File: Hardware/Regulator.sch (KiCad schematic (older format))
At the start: 8 parts, among them U2 LM1084IS-3.3/NOPB, U3 LM1084IS-5.0/NOPB

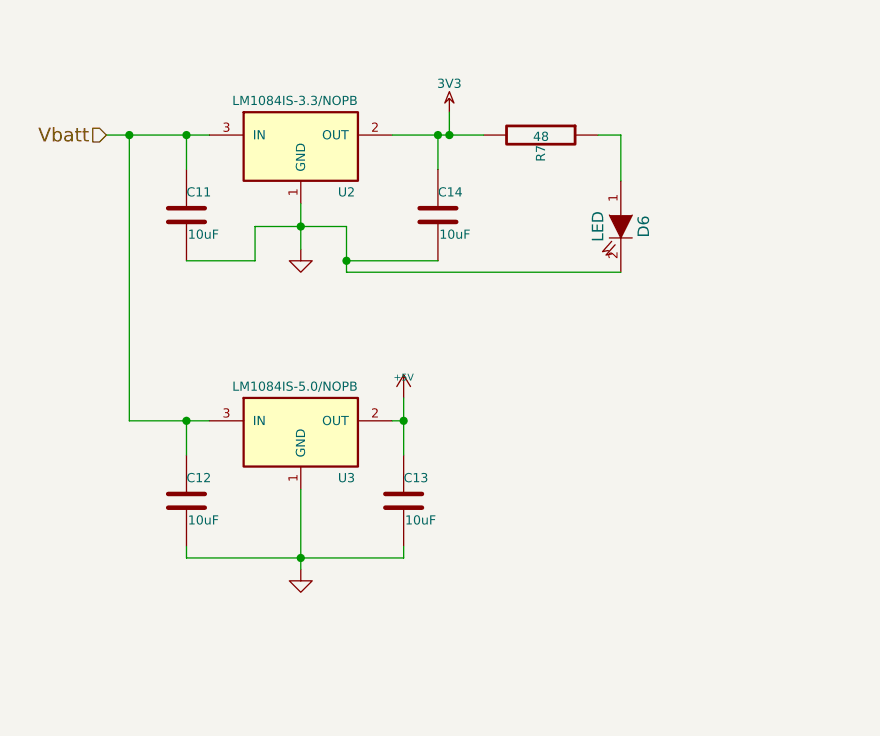
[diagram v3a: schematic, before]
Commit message: Finished schematic work. Began footprints
Began assigning footprints for R2
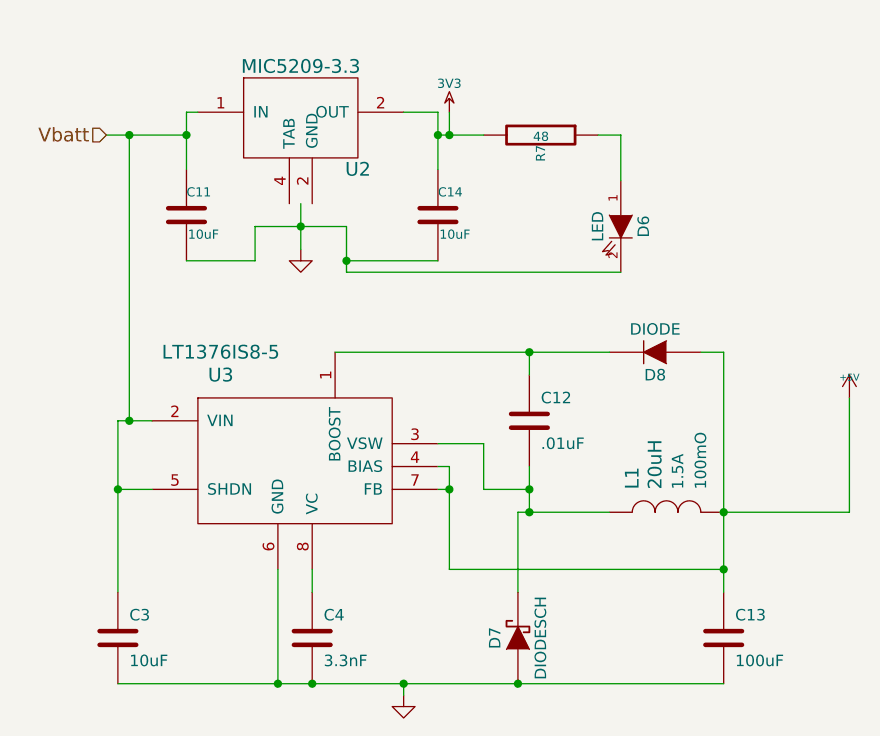
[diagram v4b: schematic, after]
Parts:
- removed U2: LM1084IS-3.3/NOPB, SMD_Packages:DPAK-3, symbol LM1084IS-3.3/NOPB
- removed U3: LM1084IS-5.0/NOPB, SMD_Packages:DPAK-3, symbol LM1084IS-5.0/NOPB
- added C3: 10uF, Capacitors_SMD:C_0805_HandSoldering, symbol C
- added C4: 3.3nF, Capacitors_SMD:C_0805_HandSoldering, symbol C
- added D7: DIODESCH, Diodes_SMD:Diode-MELF_Handsoldering, symbol DIODESCH
- added D8: DIODE, Diodes_SMD:Diode-MELF_Handsoldering, symbol DIODE
- added L1: 20uH, Capacitors_SMD:C_2220_HandSoldering, symbol Inductor
- added U2: MIC5209-3.3, SMD_Packages:DPAK-3, symbol MIC5209-3.3
- added U3: LT1376IS8-5, SMD_Packages:DPAK-3, symbol LT1376IS8-5
- C12: value 10uF -> .01uF
- C13: value 10uF -> 100uF
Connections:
- net +5V: now also D8.1 (A), L1.2, U3.4 (BIAS), U3.7 (FB)
- net 3V3: now also U2.2 (OUT)
- net GND: now also C3.2, C4.2, D7.1 (A), U3.6 (GND); no longer C12.2
- net Vbatt: now also C3.1, U2.1 (IN), U3.2 (VIN), U3.5 (SHDN); no longer C12.1
- new net: C12.2, D7.2 (K), L1.1, U3.3 (VSW)
- new net: C12.1, D8.2 (K), U3.1 (BOOST)
- new net: C4.1, U3.8 (VC)
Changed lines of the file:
@@
 $EndDescr
 $Comp
-L 3V3 #PWR018
+L 3V3 #PWR019
 U 1 1 543769E5
 P 2300 2050
-F 0 "#PWR018" H 2300 2150 40  0001 C CNN
+F 0 "#PWR019" H 2300 2150 40  0001 C CNN
 F 1 "3V3" H 2300 2175 40  0000 C CNN
 F 2 "" H 2300 2050 60  0000 C CNN
@@
 	1    0    0    -1
 $EndComp
-$Comp
-L LM1084IS-3.3/NOPB U2
-U 1 1 543769F9
-P 1650 2200
-F 0 "U2" H 1850 2000 40  0000 C CNN
-F 1 "LM1084IS-3.3/NOPB" H 1350 2400 40  0000 L CNN
-F 2 "SMD_Packages:DPAK-3" H 1650 2300 30  0001 C CIN
-F 3 "" H 1650 2200 60  0000 C CNN
-	1    1650 2200
-	1    0    0    -1
-$EndComp
 Text HLabel 800  2150 0    60   Input ~ 0
 Vbatt
 $Comp
-L GND #PWR019
+L GND #PWR020
 U 1 1 54376AC4
 P 1650 2650
-F 0 "#PWR019" H 1650 2650 30  0001 C CNN
+F 0 "#PWR020" H 1650 2650 30  0001 C CNN
 F 1 "GND" H 1650 2580 30  0001 C CNN
 F 2 "" H 1650 2650 60  0000 C CNN
@@
 $EndComp
 $Comp
-L LM1084IS-5.0/NOPB U3
-U 1 1 5444771F
-P 1650 3450
-F 0 "U3" H 1850 3250 40  0000 C CNN
-F 1 "LM1084IS-5.0/NOPB" H 1350 3650 40  0000 L CNN
-F 2 "SMD_Packages:DPAK-3" H 1650 3550 30  0001 C CIN
-F 3 "~" H 1650 3450 60  0000 C CNN
-	1    1650 3450
-	1    0    0    -1
-$EndComp
-$Comp
-L C C12
-U 1 1 5444778F
-P 1150 3750
-F 0 "C12" H 1150 3850 40  0000 L CNN
-F 1 "10uF" H 1156 3665 40  0000 L CNN
-F 2 "Capacitors_SMD:C_0805_HandSoldering" H 1188 3600 30  0001 C CNN
-F 3 "" H 1150 3750 60  0000 C CNN
-	1    1150 3750
-	1    0    0    -1
-$EndComp
-$Comp
-L GND #PWR020
-U 1 1 544477E3
-P 1650 4050
-F 0 "#PWR020" H 1650 4050 30  0001 C CNN
-F 1 "GND" H 1650 3980 30  0001 C CNN
-F 2 "" H 1650 4050 60  0000 C CNN
-F 3 "" H 1650 4050 60  0000 C CNN
-	1    1650 4050
-	1    0    0    -1
-$EndComp
-$Comp
-L C C13
-U 1 1 5444789E
-P 2100 3750
-F 0 "C13" H 2100 3850 40  0000 L CNN
-F 1 "10uF" H 2106 3665 40  0000 L CNN
-F 2 "Capacitors_SMD:C_0805_HandSoldering" H 2138 3600 30  0001 C CNN
-F 3 "" H 2100 3750 60  0000 C CNN
-	1    2100 3750
-	1    0    0    -1
-$EndComp
-$Comp
 L +5V #PWR021
 U 1 1 544485F5
-P 2100 3300
-F 0 "#PWR021" H 2100 3390 20  0001 C CNN
-F 1 "+5V" H 2100 3390 30  0000 C CNN
-F 2 "" H 2100 3300 60  0000 C CNN
-F 3 "" H 2100 3300 60  0000 C CNN
-	1    2100 3300
-	1    0    0    -1
-$EndComp
-Wire Wire Line
-	2050 2150 2450 2150
+P 4050 3300
+F 0 "#PWR021" H 4050 3390 20  0001 C CNN
+F 1 "+5V" H 4050 3390 30  0000 C CNN
+F 2 "" H 4050 3300 60  0000 C CNN
+F 3 "" H 4050 3300 60  0000 C CNN
+	1    4050 3300
+	1    0    0    -1
+$EndComp
 Wire Wire Line
 	2300 2150 2300 2050
-Wire Wire Line
-	800  2150 1250 2150
 Wire Wire Line
 	1650 2450 1650 2650
@@
 Connection ~ 1650 2550
 Wire Wire Line
-	2250 2300 2250 2150
+	2250 2050 2250 2300
 Connection ~ 2250 2150
 Wire Wire Line
@@
 Connection ~ 1850 2700
 Wire Wire Line
-	900  3400 1250 3400
-Wire Wire Line
 	900  3400 900  2150
 Connection ~ 900  2150
-Connection ~ 1150 3400
-Wire Wire Line
-	1150 3400 1150 3550
-Wire Wire Line
-	1150 4000 1150 3950
-Wire Wire Line
-	1650 3700 1650 4050
-Connection ~ 1650 4000
-Wire Wire Line
-	2100 3300 2100 3550
-Connection ~ 2100 3400
-Wire Wire Line
-	1150 2150 1150 2300
-Wire Wire Line
-	1150 4000 2100 4000
-Wire Wire Line
-	2100 4000 2100 3950
-Wire Wire Line
-	2100 3400 2050 3400
+Wire Wire Line
+	1150 2050 1150 2300
+$Comp
+L Inductor L1
+U 1 1 55057106
+P 3250 3800
+F 0 "L1" V 3100 3900 60  0000 L CNN
+F 1 "20uH" V 3200 3900 60  0000 L CNN
+F 2 "Capacitors_SMD:C_2220_HandSoldering" H 3150 3800 60  0001 C CNN
+F 3 "" H 3250 3900 60  0001 C CNN
+F 4 "Value" H 3250 3800 60  0001 C CNN "Manufacturer"
+F 5 "Value" H 3250 3800 60  0001 C CNN "Manufacturer Part #"
+F 6 "Value" H 3250 3800 60  0001 C CNN "Vendor"
+F 7 "Value" H 3250 3800 60  0001 C CNN "Vendor Part #"
+F 8 "1.5A" V 3300 3900 50  0000 L CNN "Current"
+F 9 "100mO" V 3400 3900 50  0000 L CNN "DCR"
+	1    3250 3800
+	1    0    0    -1
+$EndComp
+$Comp
+L DIODE D8
+U 1 1 550571B5
+P 3200 3100
+F 0 "D8" H 3200 3200 50  0000 C CNN
+F 1 "DIODE" H 3200 3000 50  0000 C CNN
+F 2 "Diodes_SMD:Diode-MELF_Handsoldering" H 3200 3100 60  0001 C CNN
+F 3 "" H 3200 3100 60  0000 C CNN
+	1    3200 3100
+	-1   0    0    1
+$EndComp
+$Comp
+L DIODESCH D7
+U 1 1 55057246
+P 2600 4350
+F 0 "D7" H 2600 4450 50  0000 C CNN
+F 1 "DIODESCH" H 2600 4250 50  0000 C CNN
+F 2 "Diodes_SMD:Diode-MELF_Handsoldering" H 2600 4350 60  0001 C CNN
+F 3 "" H 2600 4350 60  0000 C CNN
+	1    2600 4350
+	0    -1   -1   0
+$EndComp
+$Comp
+L C C12
+U 1 1 55057347
+P 2650 3400
+F 0 "C12" H 2700 3500 50  0000 L CNN
+F 1 ".01uF" H 2700 3300 50  0000 L CNN
+F 2 "Capacitors_SMD:C_0805_HandSoldering" H 2688 3250 30  0001 C CNN
+F 3 "" H 2650 3400 60  0000 C CNN
+	1    2650 3400
+	1    0    0    -1
+$EndComp
+$Comp
+L C C13
+U 1 1 550573D5
+P 3500 4350
+F 0 "C13" H 3550 4450 50  0000 L CNN
+F 1 "100uF" H 3550 4250 50  0000 L CNN
+F 2 "Capacitors_SMD:C_0805_HandSoldering" H 3538 4200 30  0001 C CNN
+F 3 "" H 3500 4350 60  0000 C CNN
+	1    3500 4350
+	1    0    0    -1
+$EndComp
+$Comp
+L C C4
+U 1 1 55057431
+P 1700 4350
+F 0 "C4" H 1750 4450 50  0000 L CNN
+F 1 "3.3nF" H 1750 4250 50  0000 L CNN
+F 2 "Capacitors_SMD:C_0805_HandSoldering" H 1738 4200 30  0001 C CNN
+F 3 "" H 1700 4350 60  0000 C CNN
+	1    1700 4350
+	1    0    0    -1
+$EndComp
+$Comp
+L LT1376IS8-5 U3
+U 1 1 55057ABF
+P 1550 3450
+F 0 "U3" H 1300 3700 60  0000 C CNN
+F 1 "LT1376IS8-5" H 1300 3800 60  0000 C CNN
+F 2 "SMD_Packages:DPAK-3" H 1550 3450 60  0001 C CNN
+F 3 "" H 1550 3450 60  0000 C CNN
+	1    1550 3450
+	1    0    0    -1
+$EndComp
+$Comp
+L C C3
+U 1 1 55057BE8
+P 850 4350
+F 0 "C3" H 900 4450 50  0000 L CNN
+F 1 "10uF" H 900 4250 50  0000 L CNN
+F 2 "Capacitors_SMD:C_0805_HandSoldering" H 888 4200 30  0001 C CNN
+F 3 "" H 850 4350 60  0000 C CNN
+	1    850  4350
+	1    0    0    -1
+$EndComp
+Wire Wire Line
+	3000 3100 1800 3100
+Wire Wire Line
+	2650 3200 2650 3100
+Connection ~ 2650 3100
+Wire Wire Line
+	2650 3600 2650 3800
+Wire Wire Line
+	2600 3800 3000 3800
+Wire Wire Line
+	2250 3500 2450 3500
+Wire Wire Line
+	2450 3500 2450 3700
+Wire Wire Line
+	2450 3700 2650 3700
+Connection ~ 2650 3700
+Wire Wire Line
+	2250 3600 2300 3600
+Wire Wire Line
+	2300 3600 2300 4050
+Wire Wire Line
+	2300 3700 2250 3700
+Wire Wire Line
+	2300 4050 3500 4050
+Wire Wire Line
+	3500 3100 3500 4150
+Connection ~ 2300 3700
+Connection ~ 3500 4050
+Wire Wire Line
+	3400 3100 3500 3100
+Connection ~ 3500 3800
+Wire Wire Line
+	3500 3800 4050 3800
+Wire Wire Line
+	4050 3800 4050 3300
+Wire Wire Line
+	2600 4150 2600 3800
+Connection ~ 2650 3800
+Wire Wire Line
+	1700 4150 1700 4050
+Wire Wire Line
+	1550 4050 1550 4550
+Connection ~ 1550 4550
+Connection ~ 2600 4550
+Wire Wire Line
+	850  4150 850  3400
+Wire Wire Line
+	850  3400 1000 3400
+Connection ~ 900  3400
+Wire Wire Line
+	1000 3700 850  3700
+Connection ~ 850  3700
+$Comp
+L GND #PWR022
+U 1 1 55058B68
+P 2100 4600
+F 0 "#PWR022" H 2100 4600 30  0001 C CNN
+F 1 "GND" H 2100 4530 30  0001 C CNN
+F 2 "" H 2100 4600 60  0000 C CNN
+F 3 "" H 2100 4600 60  0000 C CNN
+	1    2100 4600
+	1    0    0    -1
+$EndComp
+Wire Wire Line
+	2100 4550 2100 4600
+Connection ~ 2100 4550
+Wire Wire Line
+	850  4550 3500 4550
+Connection ~ 1700 4550
+$Comp
+L MIC5209-3.3 U2
+U 1 1 55060157
+P 1650 2050
+F 0 "U2" H 1900 1800 60  0000 C CNN
+F 1 "MIC5209-3.3" H 1650 2250 60  0000 C CNN
+F 2 "SMD_Packages:DPAK-3" H 1650 2050 60  0001 C CNN
+F 3 "" H 1650 2050 60  0000 C CNN
+	1    1650 2050
+	1    0    0    -1
+$EndComp
+Wire Wire Line
+	800  2150 1150 2150
+Wire Wire Line
+	1150 2050 1200 2050
+Wire Wire Line
+	2100 2050 2250 2050
+Wire Wire Line
+	2250 2150 2450 2150
 $EndSCHEMATC

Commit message: Finished creating footprints
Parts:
- U2: footprint SMD_Packages:DPAK-3 -> SMD_Packages:SOT-223
- U3: footprint SMD_Packages:DPAK-3 -> SMD_Packages:SOIC-8-N
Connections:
- net GND: now also U2.2 (OUT), U2.4 (TAB)
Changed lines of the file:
@@
 F 0 "U3" H 1300 3700 60  0000 C CNN
 F 1 "LT1376IS8-5" H 1300 3800 60  0000 C CNN
-F 2 "SMD_Packages:DPAK-3" H 1550 3450 60  0001 C CNN
+F 2 "SMD_Packages:SOIC-8-N" H 1550 3450 60  0001 C CNN
 F 3 "" H 1550 3450 60  0000 C CNN
 	1    1550 3450
@@
 F 0 "U2" H 1900 1800 60  0000 C CNN
 F 1 "MIC5209-3.3" H 1650 2250 60  0000 C CNN
-F 2 "SMD_Packages:DPAK-3" H 1650 2050 60  0001 C CNN
+F 2 "SMD_Packages:SOT-223" H 1600 2400 60  0000 C CNN
 F 3 "" H 1650 2050 60  0000 C CNN
 	1    1650 2050
@@
 Wire Wire Line
 	2250 2150 2450 2150
+Wire Wire Line
+	1600 2450 1700 2450
+Connection ~ 1650 2450
 $EndSCHEMATC

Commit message: Ready to begin laying out and routing
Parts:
- U3: footprint SMD_Packages:SOIC-8-N -> Housings_SOIC:SOIC-8_3.9x4.9mm_Pitch1.27mm
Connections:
- net GND: no longer U2.2 (OUT)
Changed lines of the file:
@@
 	1    0    0    -1
 $EndComp
-Wire Wire Line
-	2300 2150 2300 2050
-Wire Wire Line
-	1650 2450 1650 2650
-Connection ~ 1150 2150
-Wire Wire Line
-	1150 2700 1450 2700
-Wire Wire Line
-	1450 2700 1450 2550
-Wire Wire Line
-	1450 2550 1850 2550
-Connection ~ 1650 2550
-Wire Wire Line
-	2250 2050 2250 2300
-Connection ~ 2250 2150
-Wire Wire Line
-	2250 2700 1850 2700
-Wire Wire Line
-	1850 2550 1850 2750
-Connection ~ 2300 2150
-Wire Wire Line
-	2950 2150 3050 2150
-Wire Wire Line
-	3050 2150 3050 2350
-Wire Wire Line
-	1850 2750 3050 2750
-Connection ~ 1850 2700
-Wire Wire Line
-	900  3400 900  2150
-Connection ~ 900  2150
-Wire Wire Line
-	1150 2050 1150 2300
 $Comp
 L Inductor L1
@@
 $EndComp
 $Comp
+L C C4
+U 1 1 55057431
+P 1700 4350
+F 0 "C4" H 1750 4450 50  0000 L CNN
+F 1 "3.3nF" H 1750 4250 50  0000 L CNN
+F 2 "Capacitors_SMD:C_0805_HandSoldering" H 1738 4200 30  0001 C CNN
+F 3 "" H 1700 4350 60  0000 C CNN
+	1    1700 4350
+	1    0    0    -1
+$EndComp
+$Comp
+L LT1376IS8-5 U3
+U 1 1 55057ABF
+P 1550 3450
+F 0 "U3" H 1300 3700 60  0000 C CNN
+F 1 "LT1376IS8-5" H 1300 3800 60  0000 C CNN
+F 2 "Housings_SOIC:SOIC-8_3.9x4.9mm_Pitch1.27mm" H 1550 3450 60  0001 C CNN
+F 3 "" H 1550 3450 60  0000 C CNN
+	1    1550 3450
+	1    0    0    -1
+$EndComp
+$Comp
+L C C3
+U 1 1 55057BE8
+P 850 4350
+F 0 "C3" H 900 4450 50  0000 L CNN
+F 1 "10uF" H 900 4250 50  0000 L CNN
+F 2 "Capacitors_SMD:C_0805_HandSoldering" H 888 4200 30  0001 C CNN
+F 3 "" H 850 4350 60  0000 C CNN
+	1    850  4350
+	1    0    0    -1
+$EndComp
+$Comp
+L GND #PWR022
+U 1 1 55058B68
+P 2100 4600
+F 0 "#PWR022" H 2100 4600 30  0001 C CNN
+F 1 "GND" H 2100 4530 30  0001 C CNN
+F 2 "" H 2100 4600 60  0000 C CNN
+F 3 "" H 2100 4600 60  0000 C CNN
+	1    2100 4600
+	1    0    0    -1
+$EndComp
+$Comp
+L MIC5209-3.3 U2
+U 1 1 55060157
+P 1650 2050
+F 0 "U2" H 1900 1800 60  0000 C CNN
+F 1 "MIC5209-3.3" H 1650 2250 60  0000 C CNN
+F 2 "SMD_Packages:SOT-223" H 1600 2400 60  0000 C CNN
+F 3 "" H 1650 2050 60  0000 C CNN
+	1    1650 2050
+	1    0    0    -1
+$EndComp
+$Comp
 L C C13
 U 1 1 550573D5
@@
 	1    0    0    -1
 $EndComp
-$Comp
-L C C4
-U 1 1 55057431
-P 1700 4350
-F 0 "C4" H 1750 4450 50  0000 L CNN
-F 1 "3.3nF" H 1750 4250 50  0000 L CNN
-F 2 "Capacitors_SMD:C_0805_HandSoldering" H 1738 4200 30  0001 C CNN
-F 3 "" H 1700 4350 60  0000 C CNN
-	1    1700 4350
-	1    0    0    -1
-$EndComp
-$Comp
-L LT1376IS8-5 U3
-U 1 1 55057ABF
-P 1550 3450
-F 0 "U3" H 1300 3700 60  0000 C CNN
-F 1 "LT1376IS8-5" H 1300 3800 60  0000 C CNN
-F 2 "SMD_Packages:SOIC-8-N" H 1550 3450 60  0001 C CNN
-F 3 "" H 1550 3450 60  0000 C CNN
-	1    1550 3450
-	1    0    0    -1
-$EndComp
-$Comp
-L C C3
-U 1 1 55057BE8
-P 850 4350
-F 0 "C3" H 900 4450 50  0000 L CNN
-F 1 "10uF" H 900 4250 50  0000 L CNN
-F 2 "Capacitors_SMD:C_0805_HandSoldering" H 888 4200 30  0001 C CNN
-F 3 "" H 850 4350 60  0000 C CNN
-	1    850  4350
-	1    0    0    -1
-$EndComp
+Wire Wire Line
+	2300 2150 2300 2050
+Wire Wire Line
+	1650 2450 1650 2650
+Connection ~ 1150 2150
+Wire Wire Line
+	1150 2700 1450 2700
+Wire Wire Line
+	1450 2700 1450 2550
+Wire Wire Line
+	1450 2550 1850 2550
+Connection ~ 1650 2550
+Wire Wire Line
+	2250 2050 2250 2300
+Connection ~ 2250 2150
+Wire Wire Line
+	2250 2700 1850 2700
+Wire Wire Line
+	1850 2550 1850 2750
+Connection ~ 2300 2150
+Wire Wire Line
+	2950 2150 3050 2150
+Wire Wire Line
+	3050 2150 3050 2350
+Wire Wire Line
+	1850 2750 3050 2750
+Connection ~ 1850 2700
+Wire Wire Line
+	900  3400 900  2150
+Connection ~ 900  2150
+Wire Wire Line
+	1150 2050 1150 2300
 Wire Wire Line
 	3000 3100 1800 3100
@@
 	1000 3700 850  3700
 Connection ~ 850  3700
-$Comp
-L GND #PWR022
-U 1 1 55058B68
-P 2100 4600
-F 0 "#PWR022" H 2100 4600 30  0001 C CNN
-F 1 "GND" H 2100 4530 30  0001 C CNN
-F 2 "" H 2100 4600 60  0000 C CNN
-F 3 "" H 2100 4600 60  0000 C CNN
-	1    2100 4600
-	1    0    0    -1
-$EndComp
 Wire Wire Line
 	2100 4550 2100 4600
@@
 	850  4550 3500 4550
 Connection ~ 1700 4550
-$Comp
-L MIC5209-3.3 U2
-U 1 1 55060157
-P 1650 2050
-F 0 "U2" H 1900 1800 60  0000 C CNN
-F 1 "MIC5209-3.3" H 1650 2250 60  0000 C CNN
-F 2 "SMD_Packages:SOT-223" H 1600 2400 60  0000 C CNN
-F 3 "" H 1650 2050 60  0000 C CNN
-	1    1650 2050
-	1    0    0    -1
-$EndComp
 Wire Wire Line
 	800  2150 1150 2150
@@
 	2250 2150 2450 2150
 Wire Wire Line
-	1600 2450 1700 2450
-Connection ~ 1650 2450
+	1600 2450 1650 2450
 $EndSCHEMATC

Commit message: Began routing
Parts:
- C13: footprint Capacitors_SMD:C_0805_HandSoldering -> Local:SMD_CAP
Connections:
- net +5V: now also C11.1, U2.1 (IN)
- net GND: now also U2.2 (OUT)
- net Vbatt: no longer C11.1, U2.1 (IN)
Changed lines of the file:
@@
 F 0 "C13" H 3550 4450 50  0000 L CNN
 F 1 "100uF" H 3550 4250 50  0000 L CNN
-F 2 "Capacitors_SMD:C_0805_HandSoldering" H 3538 4200 30  0001 C CNN
+F 2 "Local:SMD_CAP" H 3538 4200 30  0001 C CNN
 F 3 "" H 3500 4350 60  0000 C CNN
 	1    3500 4350
@@
 Wire Wire Line
 	1650 2450 1650 2650
-Connection ~ 1150 2150
 Wire Wire Line
 	1150 2700 1450 2700
@@
 Connection ~ 1700 4550
 Wire Wire Line
-	800  2150 1150 2150
-Wire Wire Line
-	1150 2050 1200 2050
+	950  2050 1200 2050
 Wire Wire Line
 	2100 2050 2250 2050
@@
 	2250 2150 2450 2150
 Wire Wire Line
-	1600 2450 1650 2450
+	1600 2450 1700 2450
+Wire Wire Line
+	900  2150 800  2150
+Wire Wire Line
+	950  2050 950  2850
+Wire Wire Line
+	950  2850 3700 2850
+Wire Wire Line
+	3700 2850 3700 3500
+Wire Wire Line
+	3700 3500 4050 3500
+Connection ~ 4050 3500
+Connection ~ 1150 2050
+Connection ~ 1650 2450
 $EndSCHEMATC
